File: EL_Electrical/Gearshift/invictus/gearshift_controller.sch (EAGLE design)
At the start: 55 parts, among them IC1 MCP2562-E_SN, IC2 MCP2515-I_SO, J1 22-05-7028-02, Q1 BSS123, Q2 BSS123, Q3 BSS123, Q4 BSS123, Q5 BSS123, Q6 BSS123, Q7 BSS123

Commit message: Update of electrical schematic (4 pins from DTA extras)
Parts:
- added ALIM: 22-05-7028-02, EP_molex_6410_7395:22-05-7028-02
- added CONN_DTA: 22-05-7068-06, con-molex:22-05-7068-06
- added Q10, Q8, Q9: BSS123, transistor-small-signal:BSS123
- added R24, R25, R26, R27, R28, R29: 10k, rcl:R-EU_R0805
- CONN_MOTOR: value 22-05-7078-07 -> 22-05-7068-06; device EP_molex_6410_7395:22-05-7078-07 -> con-molex:22-05-7068-06
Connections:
- net OUT0_3.3V renamed LOG_3.3V
- net SHIFT_POT_5V renamed GEAR_POT_5V
- removed net OUT0_12V: CONN_MOTOR-5.S, Q1.D, R2.1
- removed net SHIFT_POT_3.3V: Q5.S, Q7.S, R22.1, R9.1
- new net GEAR_POT_3.3V: Q7.S, R22.1
- new net LAUNCH_CONTROL_3.3V: Q9.S, R26.1
- new net LAUNCH_CONTROL_5V: Q9.D, R27.1
- new net LOG_5V: Q1.D, R2.1
- new net N$1: CONN_DTA-1.S
- new net N$10: CONN_DTA-5.S
- new net N$12: CONN_DTA-6.S
- new net N$5: CONN_DTA-2.S
- new net N$8: CONN_DTA-3.S
- new net N$9: CONN_DTA-4.S
- new net OUT3_3.3V: Q4.S, R7.1
- new net OUT4_3.3V: Q5.S, R9.1
- new net TRACTION_CONTROL_3.3V: Q8.S, R24.1
- new net TRACTION_CONTROL_5V: Q8.D, R25.1
- new net WET/DRY_3.3V: Q10.S, R28.1
- new net WET/DRY_5V: Q10.D, R29.1
- net +12V: now also ALIM-2.S; no longer R2.2
- net +3V3: now also Q10.G, Q8.G, Q9.G, R24.2, R26.2, R28.2
- net +5V: now also R2.2, R25.2, R27.2, R29.2
- net GND: now also ALIM-1.S
- net IN0_12V: now also CONN_MOTOR-6.S; no longer CONN_MOTOR-7.S
- net IN1_12V: now also CONN_MOTOR-5.S; no longer CONN_MOTOR-6.S
- net SHIFT_CUT_3.3V: no longer Q4.S, R7.1
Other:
- note added: "DTA"
- note added: "GEAR_POT_ANALOG"
- note added: "Low Dropout Regulator (LDO)"
- note added: "Motoréductuer"
- note added: "Power supply"
- note removed: "LDO"
- moved on the sheet: C106, C107, C108, C109, CONN_MOTOR-1, CONN_MOTOR-2, CONN_MOTOR-3, CONN_MOTOR-4, CONN_MOTOR-5, CONN_MOTOR-6, I105, Q1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

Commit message: Definition of inputs/outputs in Teensy 3.2. PCB Layout Design (ground plane missing)
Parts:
- removed ECU: 22-05-7028-02, EP_molex_6410_7395:22-05-7028-02
- removed J1: 22-05-7028-02, con-molex:22-05-7028-02
- removed Q7: BSS123, transistor-small-signal:BSS123
- removed R23: 10k, rcl:R-EU_R0805
- added CONN_CAN: 22-05-7028-02, con-molex:22-05-7028-02
- C4, C5: device rcl:CPOL-EUE2,5-6E -> rcl:C-EUC0805
- CONN_DTA: value 22-05-7068-06 -> 22-05-7078-07; device con-molex:22-05-7068-06 -> con-molex:22-05-7078-07
- Q1, Q10, Q2, Q3, Q4, Q5, Q6, Q9: value BSS123 -> BSS138
- R2: value 10k -> 4k7
- R22, R25, R27, R29: value 10k -> 330
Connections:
- removed net GEAR_POT_3.3V: Q7.S, R22.1
- removed net GEAR_POT_5V: ECU-1.S, Q7.D, R23.1
- removed net N$12: CONN_DTA-6.S
- removed net N$5: CONN_DTA-2.S
- new net GEAR_POT: CONN_DTA-7.S, U$1.A14/DAC
- new net GND1: CONN_DTA-1.S, Q1.S, Q10.S, Q8.S, Q9.S, R1.1, R24.1, R26.1, R28.1
- net +3V3: no longer Q1.G, Q10.G, Q7.G, Q8.G, Q9.G, R1.2, R22.2, R24.2, R26.2, R28.2
- net +5V: no longer R23.2, R25.2, R27.2, R29.2
- net GND: now also C4.2, C5.2; no longer C4.-, C5.-
- net IN0_12V: now also CONN_MOTOR-1.S; no longer CONN_MOTOR-6.S
- net IN0_3.3V: now also U$1.8/TX3
- net IN1_12V: now also CONN_MOTOR-2.S; no longer CONN_MOTOR-5.S
- net IN1_3.3V: now also U$1.9/RX2/PWM
- net LAUNCH_CONTROL_3.3V: now also R27.2, U$1.15/A1/T; no longer Q9.S, R26.1
- net LAUNCH_CONTROL_5V: now also CONN_DTA-5.S; no longer R27.1
- net LOG_3.3V: now also R22.2, U$1.17/A3/T; no longer Q1.S, R1.1
- net LOG_5V: now also CONN_DTA-3.S
- net N$1: now also Q1.G, R1.2, R22.1; no longer CONN_DTA-1.S
- net N$10: now also Q10.G, R28.2, R29.2; no longer CONN_DTA-5.S
- net N$4: now also CONN_CAN-1.S; no longer J1-2.S
- net N$6: now also CONN_CAN-2.S; no longer J1-1.S
- net N$8: now also Q8.G, R24.2, R25.1; no longer CONN_DTA-3.S
- net N$9: now also Q9.G, R26.2, R27.1; no longer CONN_DTA-4.S
- net OUT1_12V: now also CONN_MOTOR-3.S; no longer CONN_MOTOR-4.S
- net OUT1_3.3V: now also U$1.22/A8/T/PWM
- net OUT2_12V: now also CONN_MOTOR-4.S; no longer CONN_MOTOR-3.S
- net OUT2_3.3V: now also U$1.21/A7/PWM
- net OUT3_12V: now also CONN_MOTOR-5.S; no longer CONN_MOTOR-2.S
- net OUT3_3.3V: now also U$1.20/A6/PWM
- net OUT4_12V: now also CONN_MOTOR-6.S; no longer CONN_MOTOR-1.S
- net OUT4_3.3V: now also U$1.19/A5/T/SCL0
- net PALETTE_DROITE: now also C5.1, U$1.1/TX1/T; no longer C5.+
- net PALETTE_GAUCHE: now also C4.1, U$1.0/RX1/T; no longer C4.+
- net SHIFT_CUT_3.3V: now also U$1.18/A4/T/SDA0
- net SHIFT_CUT_5V: now also CONN_DTA-2.S; no longer ECU-2.S
- net TRACTION_CONTROL_3.3V: now also R25.2, U$1.16/A2/T; no longer Q8.S, R24.1
- net TRACTION_CONTROL_5V: now also CONN_DTA-4.S; no longer R25.1
- net WET/DRY_3.3V: now also R29.1, U$1.14/A0; no longer Q10.S, R28.1
- net WET/DRY_5V: now also CONN_DTA-6.S; no longer R29.1
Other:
- moved on the sheet: ALIM-1, ALIM-2, C106, C107, C108, C109, CONN_DTA-1, CONN_DTA-2, CONN_DTA-3, CONN_DTA-4, CONN_DTA-5, CONN_DTA-6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

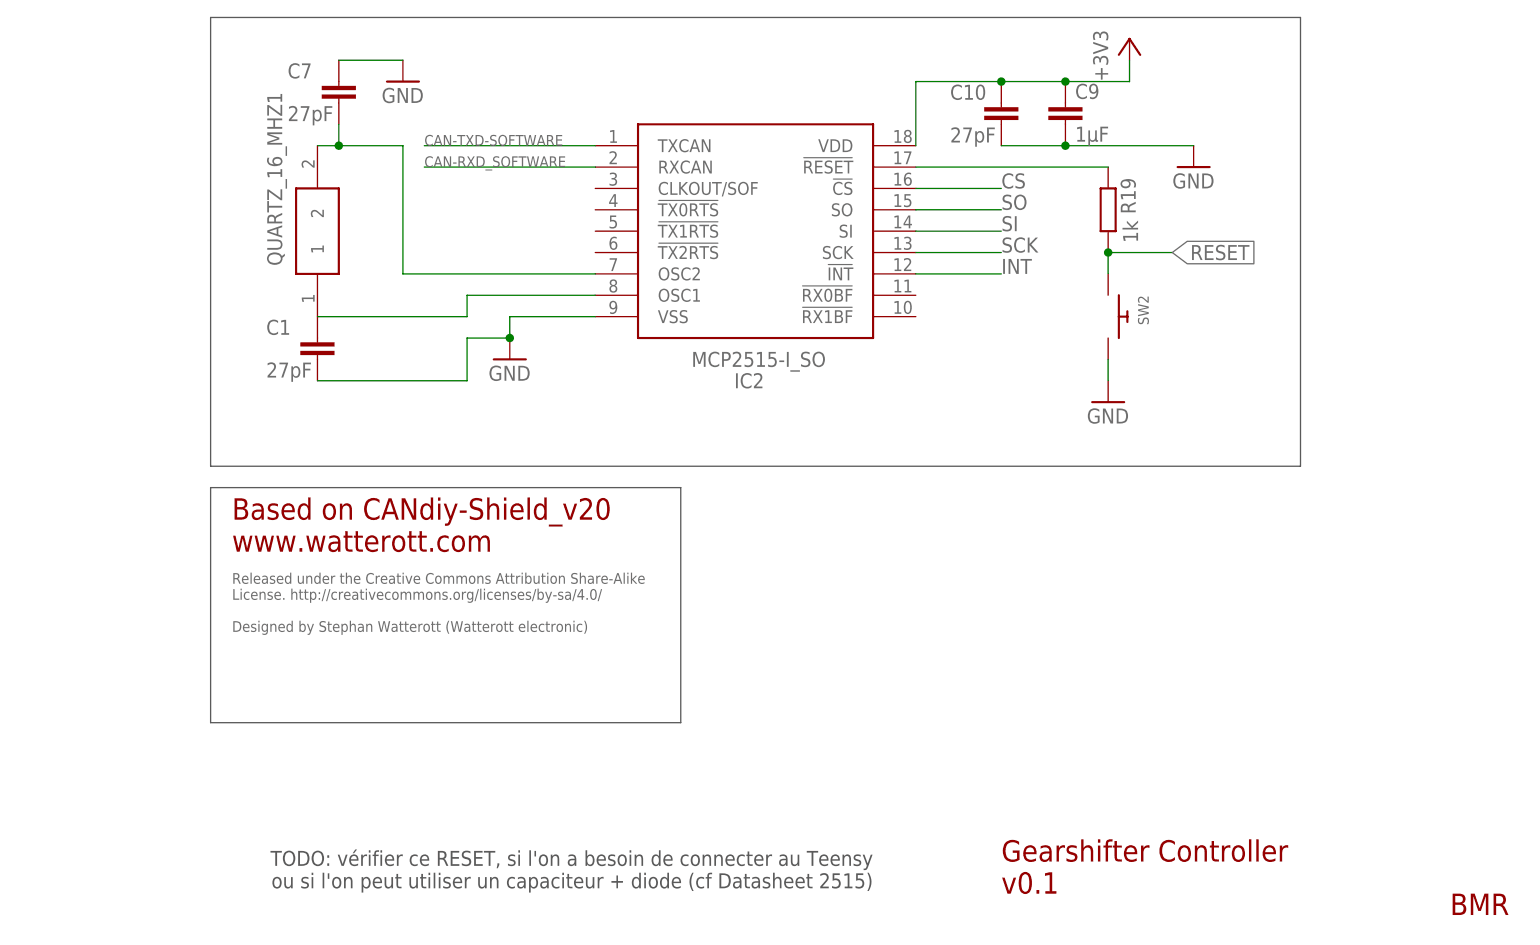
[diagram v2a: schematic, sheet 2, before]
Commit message: Update de sch et brd files (Position of connectors, minor changes)
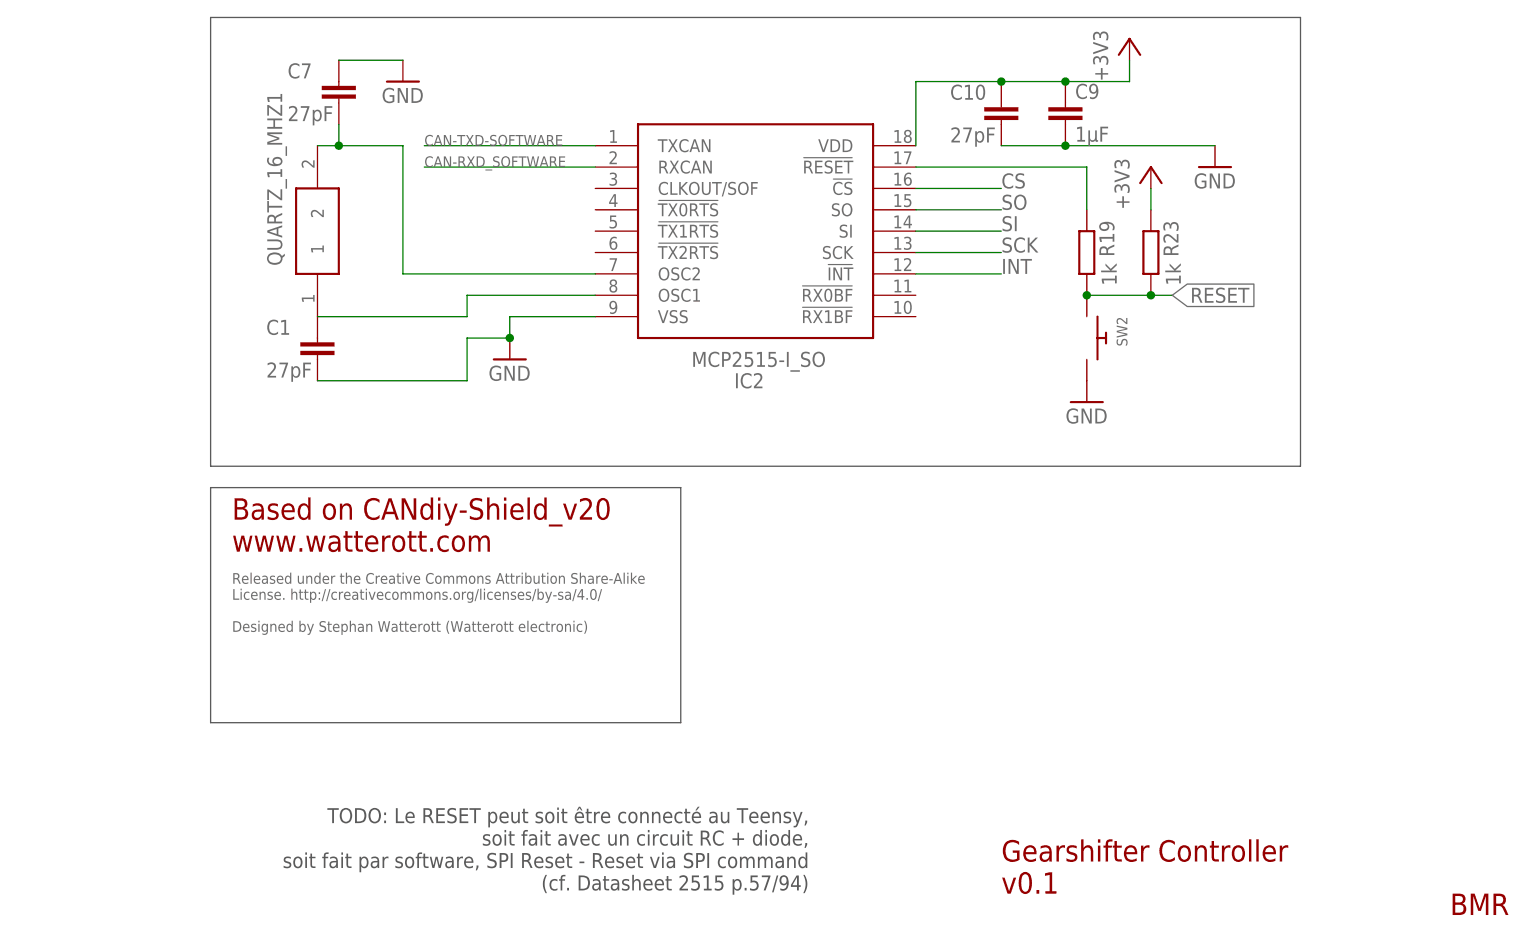
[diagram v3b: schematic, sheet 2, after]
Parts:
- added R23: 1k, rcl:R-EU_R0805
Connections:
- net +3V3: now also R23.1
- net RESET: now also R23.2
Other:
- note added: "TODO: Le RESET peut soit être connecté au Teensy, soit fait avec un circuit RC + diode, soit fait par software, SPI Reset - Reset via SPI command (cf. Datasheet 2515 p.57/94)"
- note removed: "TODO: vérifier ce RESET, si l'on a besoin de connecter au Teensy ou si l'on peut utiliser un capaciteur + diode (cf Datasheet 2515)"
- moved on the sheet: R19, SW2
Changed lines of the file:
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@@
 <part name="SUPPLY5" library="supply2" library_urn="urn:adsk.eagle:library:372" deviceset="GND1" device="" value="GND_DTA"/>
 <part name="CONN_DTA" library="con-molex" library_urn="urn:adsk.eagle:library:165" deviceset="22-?-07" device="05-7078" package3d_urn="urn:adsk.eagle:package:8078654/1"/>
+<part name="R23" library="rcl" library_urn="urn:adsk.eagle:library:334" deviceset="R-EU_" device="R0805" package3d_urn="urn:adsk.eagle:package:23553/2" value="1k"/>
+<part name="+3V1" library="supply1" library_urn="urn:adsk.eagle:library:371" deviceset="+3V3" device=""/>
 </parts>
 <sheets>
@@
 <wire x1="10.16" y1="25.4" x2="66.04" y2="25.4" width="0.1524" layer="97"/>
 <wire x1="66.04" y1="25.4" x2="66.04" y2="-2.54" width="0.1524" layer="97"/>
-<text x="88.9" y="-17.78" size="1.778" layer="97" rot="R180">TODO: vérifier ce RESET, si l'on a besoin de connecter au Teensy
- ou si l'on peut utiliser un capaciteur + diode (cf Datasheet 2515)</text>
+<text x="81.28" y="-12.7" size="1.778" layer="97" rot="R180">TODO: Le RESET peut soit être connecté au Teensy,
+ soit fait avec un circuit RC + diode,
+ soit fait par software, SPI Reset - Reset via SPI command
+(cf. Datasheet 2515 p.57/94)</text>
 <wire x1="66.04" y1="-2.54" x2="10.16" y2="-2.54" width="0.1524" layer="97"/>
 </plain>
@@
 <attribute name="NAME" x="17.78" y="72.39" size="1.778" layer="95" rot="R270" align="center-left"/>
 </instance>
-<instance part="R19" gate="G$1" x="116.84" y="58.42" smashed="yes" rot="R270">
-<attribute name="NAME" x="118.3386" y="62.23" size="1.778" layer="95" rot="R270"/>
-<attribute name="VALUE" x="118.618" y="57.15" size="1.778" layer="96" rot="R270"/>
-</instance>
-<instance part="SW2" gate="G$1" x="116.84" y="45.72" smashed="yes" rot="R270">
-<attribute name="NAME" x="120.396" y="48.26" size="1.27" layer="95" rot="R270"/>
-<attribute name="VALUE" x="114.554" y="48.26" size="1.27" layer="96" rot="R270"/>
-</instance>
-<instance part="GND11" gate="1" x="127" y="63.5" smashed="yes">
-<attribute name="VALUE" x="124.46" y="60.96" size="1.778" layer="96"/>
+<instance part="R19" gate="G$1" x="114.3" y="53.34" smashed="yes" rot="R270">
+<attribute name="NAME" x="115.7986" y="57.15" size="1.778" layer="95" rot="R270"/>
+<attribute name="VALUE" x="116.078" y="52.07" size="1.778" layer="96" rot="R270"/>
+</instance>
+<instance part="SW2" gate="G$1" x="114.3" y="43.18" smashed="yes" rot="R270">
+<attribute name="NAME" x="117.856" y="45.72" size="1.27" layer="95" rot="R270"/>
+<attribute name="VALUE" x="112.014" y="45.72" size="1.27" layer="96" rot="R270"/>
+</instance>
+<instance part="GND11" gate="1" x="129.54" y="63.5" smashed="yes">
+<attribute name="VALUE" x="127" y="60.96" size="1.778" layer="96"/>
 </instance>
 <instance part="C1" gate="G$1" x="22.86" y="43.18" smashed="yes">
@@
 <attribute name="VALUE" x="30.48" y="71.12" size="1.778" layer="96"/>
 </instance>
-<instance part="GND13" gate="1" x="116.84" y="35.56" smashed="yes">
-<attribute name="VALUE" x="114.3" y="33.02" size="1.778" layer="96"/>
+<instance part="GND13" gate="1" x="114.3" y="35.56" smashed="yes">
+<attribute name="VALUE" x="111.76" y="33.02" size="1.778" layer="96"/>
 </instance>
 <instance part="FRAME2" gate="G$1" x="-60.96" y="-35.56" smashed="yes">
@@
 <instance part="+3V7" gate="G$1" x="119.38" y="78.74" smashed="yes">
 <attribute name="VALUE" x="116.84" y="73.66" size="1.778" layer="96" rot="R90"/>
+</instance>
+<instance part="R23" gate="G$1" x="121.92" y="53.34" smashed="yes" rot="R270">
+<attribute name="NAME" x="123.4186" y="57.15" size="1.778" layer="95" rot="R270"/>
+<attribute name="VALUE" x="123.698" y="52.07" size="1.778" layer="96" rot="R270"/>
+</instance>
+<instance part="+3V1" gate="G$1" x="121.92" y="63.5" smashed="yes">
+<attribute name="VALUE" x="119.38" y="58.42" size="1.778" layer="96" rot="R90"/>
 </instance>
 </instances>
@@
 <wire x1="104.14" y1="66.04" x2="111.76" y2="66.04" width="0.1524" layer="91"/>
 <pinref part="GND11" gate="1" pin="GND"/>
-<wire x1="127" y1="66.04" x2="111.76" y2="66.04" width="0.1524" layer="91"/>
+<wire x1="129.54" y1="66.04" x2="111.76" y2="66.04" width="0.1524" layer="91"/>
 <junction x="111.76" y="66.04"/>
 </segment>
@@
 <pinref part="SW2" gate="G$1" pin="P$2"/>
 <pinref part="GND13" gate="1" pin="GND"/>
-<wire x1="116.84" y1="40.64" x2="116.84" y2="38.1" width="0.1524" layer="91"/>
 </segment>
 </net>
@@
 <net name="N$11" class="0">
 <segment>
-<wire x1="93.98" y1="63.5" x2="116.84" y2="63.5" width="0.1524" layer="91"/>
 <pinref part="IC2" gate="G$1" pin="!RESET"/>
 <pinref part="R19" gate="G$1" pin="1"/>
+<wire x1="114.3" y1="58.42" x2="114.3" y2="63.5" width="0.1524" layer="91"/>
+<wire x1="114.3" y1="63.5" x2="93.98" y2="63.5" width="0.1524" layer="91"/>
 </segment>
 </net>
@@
 <pinref part="R19" gate="G$1" pin="2"/>
 <pinref part="SW2" gate="G$1" pin="P$1"/>
-<wire x1="116.84" y1="53.34" x2="116.84" y2="50.8" width="0.1524" layer="91"/>
-<label x="124.46" y="53.34" size="1.778" layer="95" xref="yes"/>
-<wire x1="116.84" y1="53.34" x2="124.46" y2="53.34" width="0.1524" layer="91"/>
-<junction x="116.84" y="53.34"/>
+<label x="124.46" y="48.26" size="1.778" layer="95" xref="yes"/>
+<wire x1="114.3" y1="48.26" x2="121.92" y2="48.26" width="0.1524" layer="91"/>
+<junction x="114.3" y="48.26"/>
+<pinref part="R23" gate="G$1" pin="2"/>
+<wire x1="121.92" y1="48.26" x2="124.46" y2="48.26" width="0.1524" layer="91"/>
+<junction x="121.92" y="48.26"/>
 </segment>
 </net>
@@
 <pinref part="+3V7" gate="G$1" pin="+3V3"/>
 </segment>
-</net>
+<segment>
+<pinref part="R23" gate="G$1" pin="1"/>
+<pinref part="+3V1" gate="G$1" pin="+3V3"/>
+<wire x1="121.92" y1="58.42" x2="121.92" y2="60.96" width="0.1524" layer="91"/>
+</segment>
+</net>
